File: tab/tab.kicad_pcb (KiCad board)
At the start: 2 copper layers, 29 x 17.8 mm, 14 parts

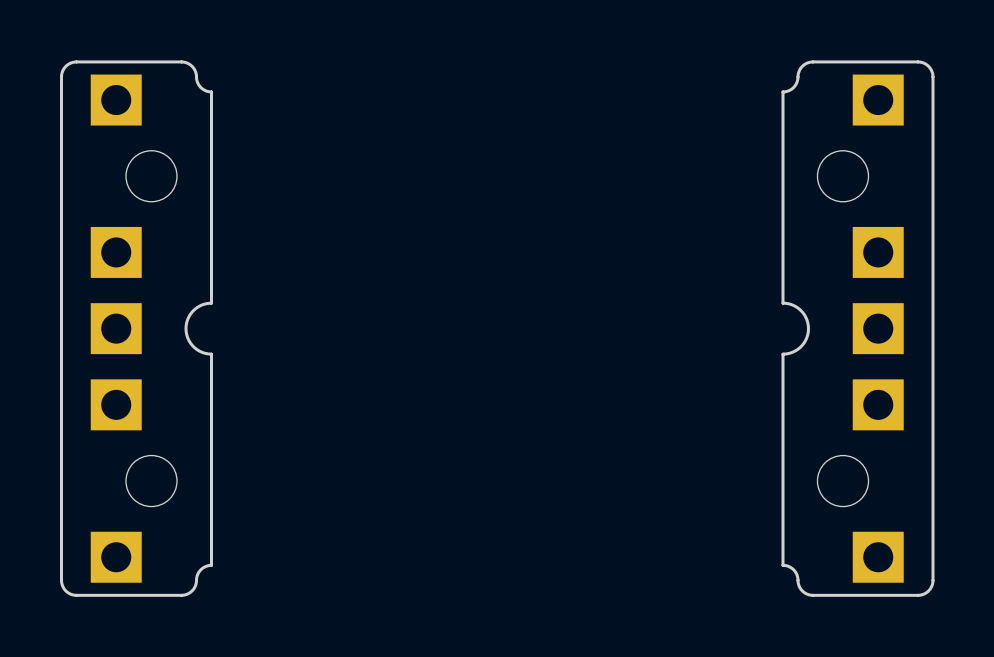
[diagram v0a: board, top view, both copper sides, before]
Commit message: make the 1u taller by a tiny bit
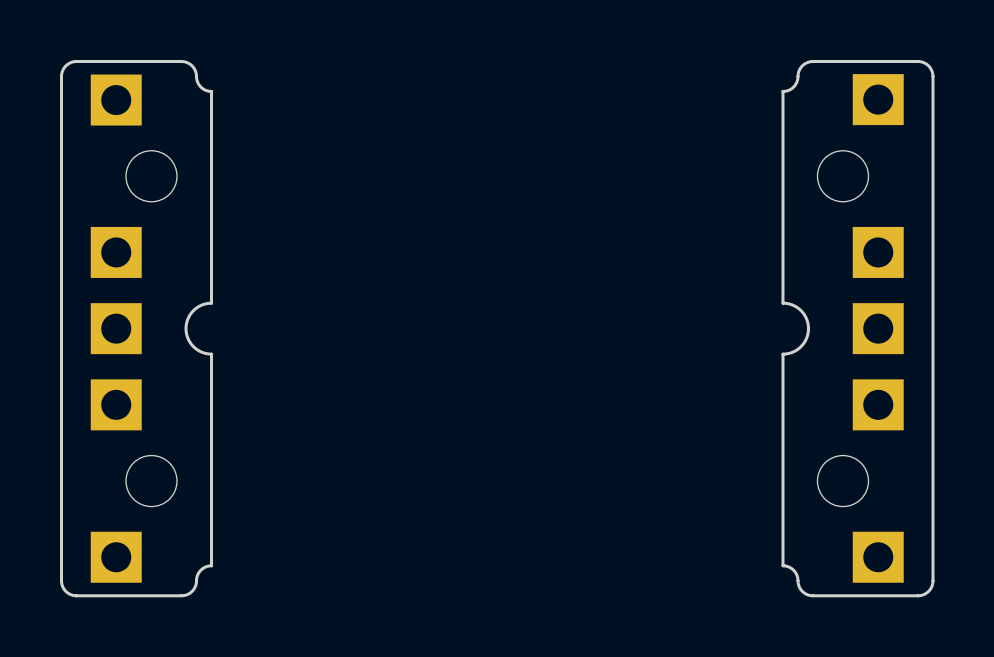
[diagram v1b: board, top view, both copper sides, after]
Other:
- outline, holes or cut-outs redrawn
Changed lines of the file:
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@@
   )
   (footprint "" (layer "F.Cu")
-    (at 106.68 71.12 90)
+    (at 106.68 71.105 90)
     (fp_text reference "" (at 0 0 90) (layer "F.SilkS")
         (effects (font (size 1.27 1.27) (thickness 0.15)))
@@
   (footprint "" (layer "F.Cu")
     (at 81.28 71.12 -90)
-    (fp_text reference "" (at 0 0 90) (layer "F.SilkS")
+    (fp_text reference "" (at -0.015 0 90) (layer "F.SilkS")
         (effects (font (size 1.27 1.27) (thickness 0.15)))
     )
-    (fp_text value "" (at 0 0 90) (layer "F.SilkS")
+    (fp_text value "" (at -0.015 0 90) (layer "F.SilkS")
         (effects (font (size 1.27 1.27) (thickness 0.15)))
     )
@@
     (pad "1" thru_hole rect (at 0 0 180) (size 1.7 1.7) (drill 1) (layers "*.Cu" "*.Mask"))
   )
-  (gr_arc (start 83.455 69.85) (mid 83.808554 69.996446) (end 83.955 70.35)
+  (gr_line (start 103.505 79.59) (end 103.505 86.645)
     (stroke (width 0.1) (type default)) (layer "Edge.Cuts"))
-  (gr_line (start 83.455 69.85) (end 79.955 69.85)
+  (gr_arc (start 83.455 69.835) (mid 83.808553 69.981447) (end 83.955 70.335)
     (stroke (width 0.1) (type default)) (layer "Edge.Cuts"))
-  (gr_arc (start 84.455 70.85) (mid 84.101447 70.703553) (end 83.955 70.35)
+  (gr_line (start 83.455 69.835) (end 79.955 69.835)
     (stroke (width 0.1) (type default)) (layer "Edge.Cuts"))
-  (gr_line (start 108.005 69.85) (end 104.505 69.85)
+  (gr_arc (start 84.455 70.835) (mid 84.101447 70.688553) (end 83.955 70.335)
     (stroke (width 0.1) (type default)) (layer "Edge.Cuts"))
-  (gr_arc (start 104.005 70.35) (mid 104.151447 69.996447) (end 104.505 69.85)
+  (gr_line (start 108.005 69.835) (end 104.505 69.835)
     (stroke (width 0.1) (type default)) (layer "Edge.Cuts"))
-  (gr_line (start 103.505 77.89) (end 103.505 70.85)
+  (gr_arc (start 104.005 70.335) (mid 104.151447 69.981447) (end 104.505 69.835)
     (stroke (width 0.1) (type default)) (layer "Edge.Cuts"))
-  (gr_arc (start 79.455 70.35) (mid 79.601447 69.996447) (end 79.955 69.85)
+  (gr_arc (start 79.455 70.335) (mid 79.601447 69.981447) (end 79.955 69.835)
     (stroke (width 0.1) (type default)) (layer "Edge.Cuts"))
-  (gr_arc (start 83.955 87.13) (mid 83.808553 87.483553) (end 83.455 87.63)
-    (stroke (width 0.1) (type default)) (layer "Edge.Cuts"))
-  (gr_line (start 84.455 70.85) (end 84.455 77.89)
+  (gr_arc (start 83.955 87.145) (mid 83.808553 87.498553) (end 83.455 87.645)
     (stroke (width 0.1) (type default)) (layer "Edge.Cuts"))
   (gr_arc (start 103.505 77.89) (mid 104.355 78.74) (end 103.505 79.59)
     (stroke (width 0.1) (type default)) (layer "Edge.Cuts"))
-  (gr_line (start 103.505 86.63) (end 103.505 79.59)
+  (gr_arc (start 79.955 87.645) (mid 79.601447 87.498553) (end 79.455 87.145)
     (stroke (width 0.1) (type default)) (layer "Edge.Cuts"))
-  (gr_line (start 84.455 79.59) (end 84.455 86.63)
-    (stroke (width 0.1) (type default)) (layer "Edge.Cuts"))
-  (gr_arc (start 79.955 87.63) (mid 79.601447 87.483553) (end 79.455 87.13)
-    (stroke (width 0.1) (type default)) (layer "Edge.Cuts"))
-  (gr_line (start 104.505 87.63) (end 108.005 87.63)
+  (gr_line (start 104.505 87.645) (end 108.005 87.645)
     (stroke (width 0.1) (type default)) (layer "Edge.Cuts"))
   (gr_arc (start 84.455 79.59) (mid 83.605 78.74) (end 84.455 77.89)
     (stroke (width 0.1) (type default)) (layer "Edge.Cuts"))
-  (gr_line (start 83.455 87.63) (end 79.955 87.63)
+  (gr_line (start 83.455 87.645) (end 79.955 87.645)
     (stroke (width 0.1) (type default)) (layer "Edge.Cuts"))
-  (gr_line (start 79.455 87.13) (end 79.455 70.35)
+  (gr_line (start 103.505 70.835) (end 103.505 77.89)
     (stroke (width 0.1) (type default)) (layer "Edge.Cuts"))
-  (gr_arc (start 104.005 70.35) (mid 103.858553 70.703553) (end 103.505 70.85)
+  (gr_line (start 84.455 70.835) (end 84.455 77.89)
     (stroke (width 0.1) (type default)) (layer "Edge.Cuts"))
-  (gr_arc (start 108.505 87.13) (mid 108.358553 87.483553) (end 108.005 87.63)
+  (gr_line (start 79.455 87.145) (end 79.455 70.335)
     (stroke (width 0.1) (type default)) (layer "Edge.Cuts"))
-  (gr_line (start 108.505 70.35) (end 108.505 87.13)
+  (gr_arc (start 104.005 70.335) (mid 103.858553 70.688553) (end 103.505 70.835)
     (stroke (width 0.1) (type default)) (layer "Edge.Cuts"))
-  (gr_arc (start 83.955 87.13) (mid 84.101447 86.776447) (end 84.455 86.63)
+  (gr_arc (start 108.505 87.145) (mid 108.358553 87.498553) (end 108.005 87.645)
     (stroke (width 0.1) (type default)) (layer "Edge.Cuts"))
-  (gr_arc (start 108.005 69.85) (mid 108.358553 69.996447) (end 108.505 70.35)
+  (gr_line (start 108.505 70.335) (end 108.505 87.145)
     (stroke (width 0.1) (type default)) (layer "Edge.Cuts"))
-  (gr_arc (start 103.505 86.63) (mid 103.858553 86.776447) (end 104.005 87.13)
+  (gr_arc (start 83.955 87.145) (mid 84.101447 86.791447) (end 84.455 86.645)
     (stroke (width 0.1) (type default)) (layer "Edge.Cuts"))
-  (gr_arc (start 104.505 87.63) (mid 104.151447 87.483553) (end 104.005 87.13)
+  (gr_arc (start 108.005 69.835) (mid 108.358553 69.981447) (end 108.505 70.335)
+    (stroke (width 0.1) (type default)) (layer "Edge.Cuts"))
+  (gr_line (start 84.455 79.59) (end 84.455 86.645)
+    (stroke (width 0.1) (type default)) (layer "Edge.Cuts"))
+  (gr_arc (start 103.505 86.645) (mid 103.858553 86.791447) (end 104.005 87.145)
+    (stroke (width 0.1) (type default)) (layer "Edge.Cuts"))
+  (gr_arc (start 104.505 87.645) (mid 104.151447 87.498553) (end 104.005 87.145)
     (stroke (width 0.1) (type default)) (layer "Edge.Cuts"))
   (gr_text "Short     R1&2\n to share GND" (at 105.94 74.465 90) (layer "B.SilkS")

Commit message: converts to 19.05x19.05mm
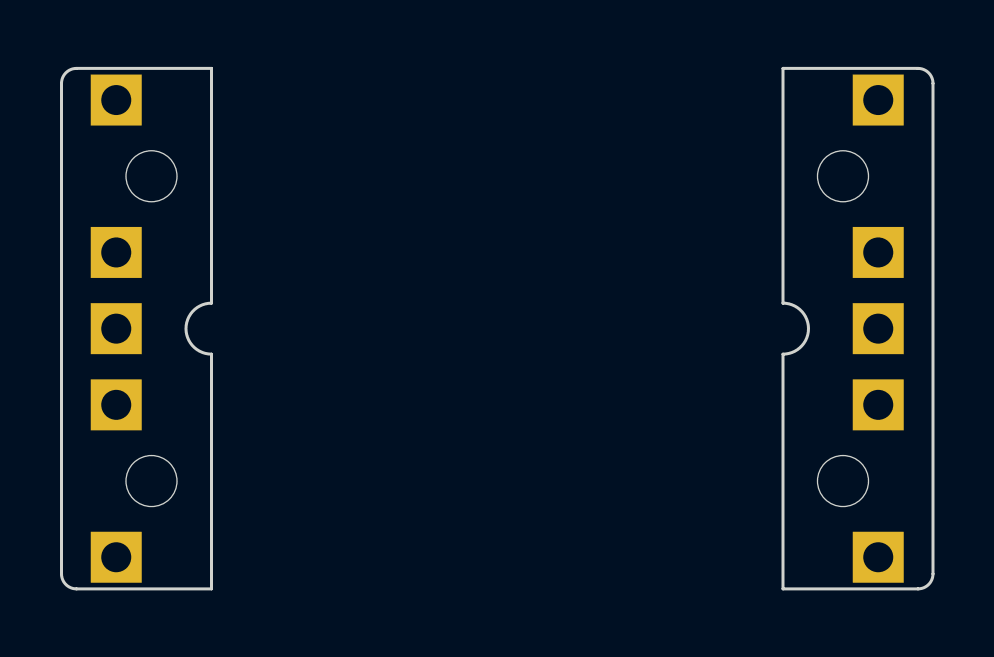
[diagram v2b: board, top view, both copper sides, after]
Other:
- board size 29 x 17.8 mm -> 29 x 17.4 mm
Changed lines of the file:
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@@
   )
   (footprint "" (layer "F.Cu")
-    (at 106.68 71.105 90)
+    (at 106.68 71.12 90)
     (fp_text reference "" (at 0 0 90) (layer "F.SilkS")
         (effects (font (size 1.27 1.27) (thickness 0.15)))
@@
     (pad "1" thru_hole rect (at 0 0 180) (size 1.7 1.7) (drill 1) (layers "*.Cu" "*.Mask"))
   )
-  (gr_line (start 103.505 79.59) (end 103.505 86.645)
+  (gr_line (start 103.505 70.065) (end 103.505 77.89)
     (stroke (width 0.1) (type default)) (layer "Edge.Cuts"))
-  (gr_arc (start 83.455 69.835) (mid 83.808553 69.981447) (end 83.955 70.335)
+  (gr_line (start 84.455 70.065) (end 79.955 70.065)
     (stroke (width 0.1) (type default)) (layer "Edge.Cuts"))
-  (gr_line (start 83.455 69.835) (end 79.955 69.835)
+  (gr_line (start 108.005 70.065) (end 103.505 70.065)
     (stroke (width 0.1) (type default)) (layer "Edge.Cuts"))
-  (gr_arc (start 84.455 70.835) (mid 84.101447 70.688553) (end 83.955 70.335)
+  (gr_arc (start 79.455 70.565) (mid 79.601447 70.211447) (end 79.955 70.065)
     (stroke (width 0.1) (type default)) (layer "Edge.Cuts"))
-  (gr_line (start 108.005 69.835) (end 104.505 69.835)
+  (gr_line (start 108.005 87.415) (end 103.505 87.415)
     (stroke (width 0.1) (type default)) (layer "Edge.Cuts"))
-  (gr_arc (start 104.005 70.335) (mid 104.151447 69.981447) (end 104.505 69.835)
-    (stroke (width 0.1) (type default)) (layer "Edge.Cuts"))
-  (gr_arc (start 79.455 70.335) (mid 79.601447 69.981447) (end 79.955 69.835)
-    (stroke (width 0.1) (type default)) (layer "Edge.Cuts"))
-  (gr_arc (start 83.955 87.145) (mid 83.808553 87.498553) (end 83.455 87.645)
+  (gr_line (start 103.505 79.59) (end 103.505 87.415)
     (stroke (width 0.1) (type default)) (layer "Edge.Cuts"))
   (gr_arc (start 103.505 77.89) (mid 104.355 78.74) (end 103.505 79.59)
     (stroke (width 0.1) (type default)) (layer "Edge.Cuts"))
-  (gr_arc (start 79.955 87.645) (mid 79.601447 87.498553) (end 79.455 87.145)
-    (stroke (width 0.1) (type default)) (layer "Edge.Cuts"))
-  (gr_line (start 104.505 87.645) (end 108.005 87.645)
+  (gr_arc (start 79.955 87.415) (mid 79.601447 87.268553) (end 79.455 86.915)
     (stroke (width 0.1) (type default)) (layer "Edge.Cuts"))
   (gr_arc (start 84.455 79.59) (mid 83.605 78.74) (end 84.455 77.89)
     (stroke (width 0.1) (type default)) (layer "Edge.Cuts"))
-  (gr_line (start 83.455 87.645) (end 79.955 87.645)
+  (gr_line (start 84.455 87.415) (end 79.955 87.415)
     (stroke (width 0.1) (type default)) (layer "Edge.Cuts"))
-  (gr_line (start 103.505 70.835) (end 103.505 77.89)
+  (gr_line (start 84.455 70.065) (end 84.455 77.89)
     (stroke (width 0.1) (type default)) (layer "Edge.Cuts"))
-  (gr_line (start 84.455 70.835) (end 84.455 77.89)
+  (gr_line (start 79.455 86.915) (end 79.455 70.565)
     (stroke (width 0.1) (type default)) (layer "Edge.Cuts"))
-  (gr_line (start 79.455 87.145) (end 79.455 70.335)
+  (gr_arc (start 108.505 86.915) (mid 108.358553 87.268553) (end 108.005 87.415)
     (stroke (width 0.1) (type default)) (layer "Edge.Cuts"))
-  (gr_arc (start 104.005 70.335) (mid 103.858553 70.688553) (end 103.505 70.835)
+  (gr_line (start 108.505 70.565) (end 108.505 86.915)
     (stroke (width 0.1) (type default)) (layer "Edge.Cuts"))
-  (gr_arc (start 108.505 87.145) (mid 108.358553 87.498553) (end 108.005 87.645)
+  (gr_arc (start 108.005 70.065) (mid 108.358553 70.211447) (end 108.505 70.565)
     (stroke (width 0.1) (type default)) (layer "Edge.Cuts"))
-  (gr_line (start 108.505 70.335) (end 108.505 87.145)
-    (stroke (width 0.1) (type default)) (layer "Edge.Cuts"))
-  (gr_arc (start 83.955 87.145) (mid 84.101447 86.791447) (end 84.455 86.645)
-    (stroke (width 0.1) (type default)) (layer "Edge.Cuts"))
-  (gr_arc (start 108.005 69.835) (mid 108.358553 69.981447) (end 108.505 70.335)
-    (stroke (width 0.1) (type default)) (layer "Edge.Cuts"))
-  (gr_line (start 84.455 79.59) (end 84.455 86.645)
-    (stroke (width 0.1) (type default)) (layer "Edge.Cuts"))
-  (gr_arc (start 103.505 86.645) (mid 103.858553 86.791447) (end 104.005 87.145)
-    (stroke (width 0.1) (type default)) (layer "Edge.Cuts"))
-  (gr_arc (start 104.505 87.645) (mid 104.151447 87.498553) (end 104.005 87.145)
+  (gr_line (start 84.455 79.59) (end 84.455 87.415)
     (stroke (width 0.1) (type default)) (layer "Edge.Cuts"))
   (gr_text "Short     R1&2\n to share GND" (at 105.94 74.465 90) (layer "B.SilkS")

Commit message: change silkscreen
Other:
- board text added: "..."
- board text added: "... short R3"
- board text added: "To share GND"
- board text added: "To share VDD"
- board text added: "short R1&2"
- board text removed: "Short R1&2 to share GND"
- board text removed: "Short R3 to share VDD"
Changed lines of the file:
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@@
   (gr_line (start 84.455 79.59) (end 84.455 87.415)
     (stroke (width 0.1) (type default)) (layer "Edge.Cuts"))
-  (gr_text "Short     R1&2\n to share GND" (at 105.94 74.465 90) (layer "B.SilkS")
+  (gr_text "..." (at 104.1 83.4 -90) (layer "B.SilkS")
     (effects (font (size 0.8 0.8) (thickness 0.15)) (justify left bottom mirror))
   )
-  (gr_text "Short     R3\n to share VDD" (at 82.02 83.015 270) (layer "B.SilkS")
+  (gr_text "... short R3" (at 83.3 74.9 90) (layer "B.SilkS")
     (effects (font (size 0.8 0.8) (thickness 0.15)) (justify left bottom mirror))
   )
+  (gr_text "short R1&2" (at 104.6 82.3 -90) (layer "B.SilkS")
+    (effects (font (size 0.8 0.8) (thickness 0.15)) (justify left bottom mirror))
+  )
+  (gr_text "..." (at 104.1 82.6 -90) (layer "F.SilkS")
+    (effects (font (size 0.8 0.8) (thickness 0.15)) (justify left bottom))
+  )
+  (gr_text "..." (at 83.8 74.7 90) (layer "F.SilkS")
+    (effects (font (size 0.8 0.8) (thickness 0.15)) (justify left bottom))
+  )
+  (gr_text "To share GND" (at 104.7 74.6 270) (layer "F.SilkS")
+    (effects (font (size 0.8 0.8) (thickness 0.15)) (justify left bottom))
+  )
+  (gr_text "To share VDD" (at 83.2 82.7 90) (layer "F.SilkS")
+    (effects (font (size 0.8 0.8) (thickness 0.15)) (justify left bottom))
+  )
 )
